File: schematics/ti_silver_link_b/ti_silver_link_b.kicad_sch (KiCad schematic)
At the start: 42 parts, among them P1 Conn_1x5, U1 24LC64, U2 TPS71533__SC70, U3 TUSB3410, U4 IMH8A, Y1 12MHz

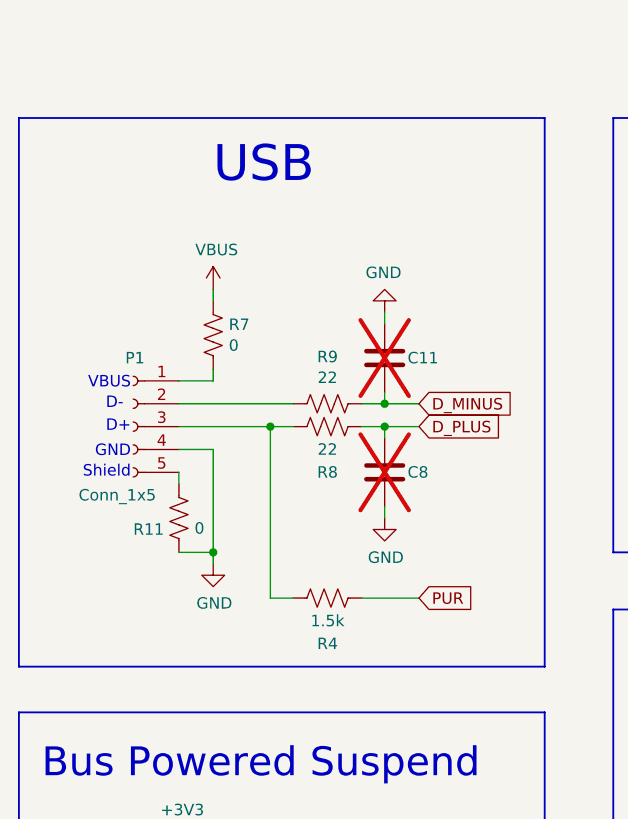
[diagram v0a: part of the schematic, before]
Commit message: Add footprints to "B" schematic's components and add initial pcb layout
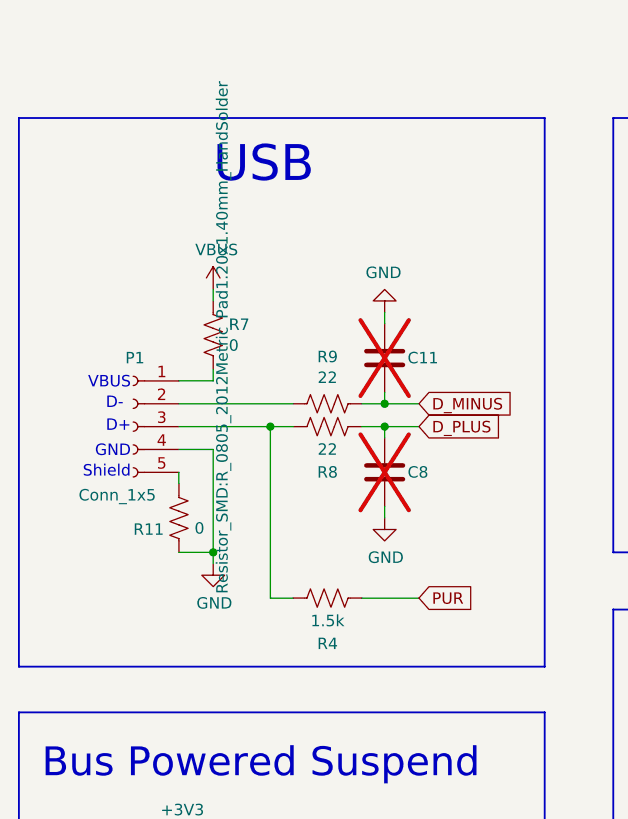
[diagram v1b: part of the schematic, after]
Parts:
- C1, C10, C11, C2, C3, C4, C5, C7, C8, C9: footprint (none) -> Capacitor_SMD:C_0805_2012Metric_Pad1.18x1.45mm_HandSolder
- D1: footprint (none) -> Package_TO_SOT_SMD:SOT-753
- L1, L2: footprint (none) -> Inductor_SMD:L_0805_2012Metric_Pad1.05x1.20mm_HandSolder
- P1: footprint (none) -> Connector_PinHeader_2.54mm:PinHeader_1x05_P2.54mm_Vertical
- R1, R10, R11, R2, R20, R21, R24, R25, R26, R27, R28, R29, R30, R4, R5, R6, R7, R8, R9: footprint (none) -> Resistor_SMD:R_0805_2012Metric_Pad1.20x1.40mm_HandSolder
- TI1: footprint (none) -> Connector_PinHeader_2.54mm:PinHeader_1x03_P2.54mm_Vertical
- TP1, TP2: footprint (none) -> TestPoint:TestPoint_Pad_D1.0mm
- U3: footprint Package_DFN_QFN:VQFN-32-1EP_5x5mm_P0.5mm_EP3.5x3.5mm_ThermalVias -> Package_QFP:LQFP-32_7x7mm_P0.8mm
- U4: footprint (none) -> Package_TO_SOT_SMD:SOT-457
- Y1: footprint (none) -> Crystal:Crystal_SMD_HC49-SD

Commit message: Update and fix "B" schematic's footprints and layout
Wrong pinout was used in U4 and D1
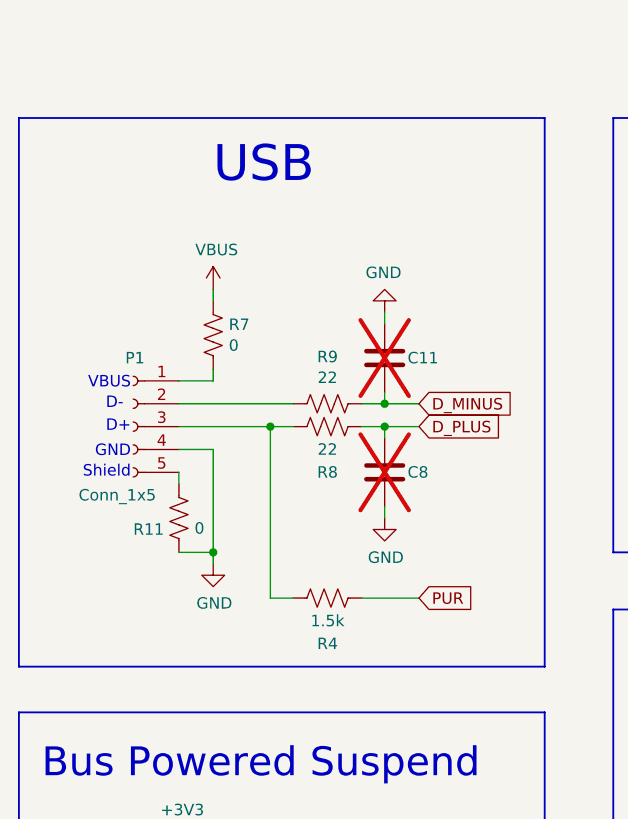
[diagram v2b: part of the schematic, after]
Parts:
- D1: footprint Package_TO_SOT_SMD:SOT-753 -> ti_graph_link_library:SOT-25_HandSoldering_clockwise_pin_numbering
- U4: footprint Package_TO_SOT_SMD:SOT-457 -> Package_TO_SOT_SMD:ROHM_SOT-457_ClockwisePinNumbering

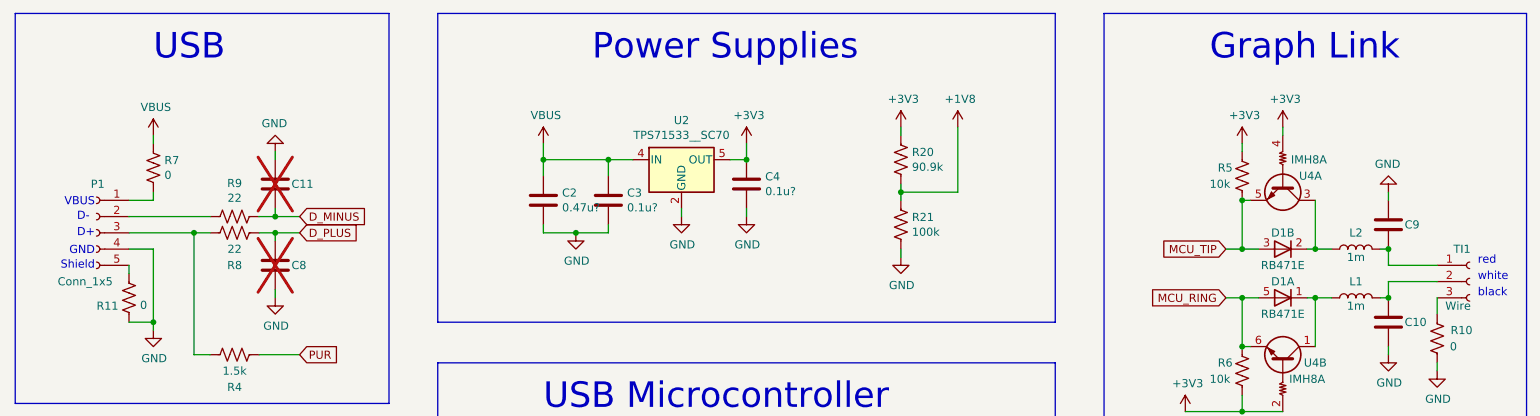
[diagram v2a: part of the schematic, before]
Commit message: Add USB and audio jack connectors to "B" schematic and pcb layout
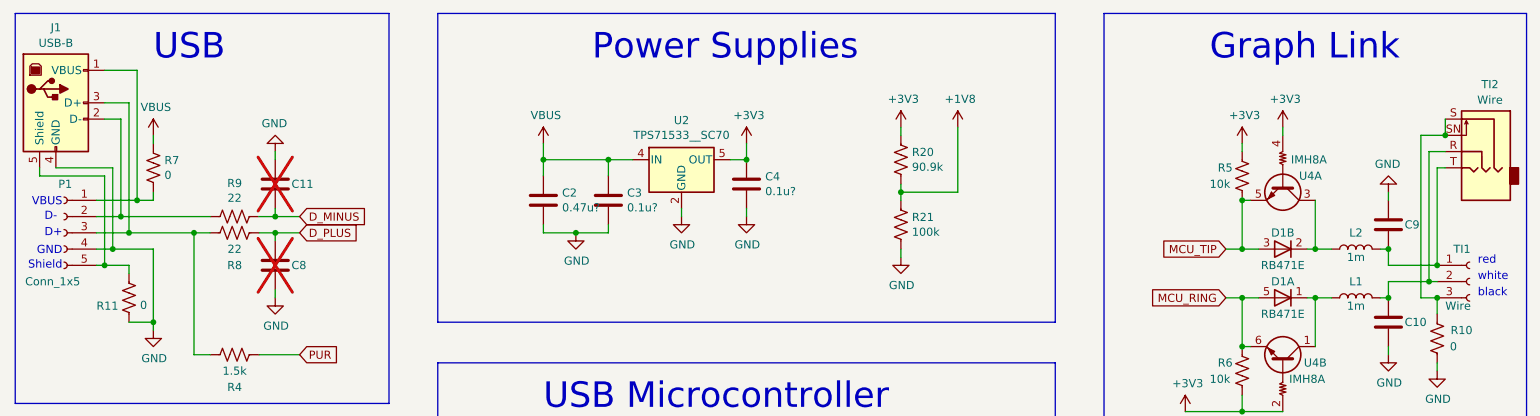
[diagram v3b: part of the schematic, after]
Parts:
- added J1: USB-B, ti_graph_link_library:USB_B_Logitech_C270_cable_connector, symbol ti_graph_link:USB-B
- added TI2: Wire, ti_graph_link_library:Jack_2.5mm_with_switch-SMT_Horizontal, symbol ti_graph_link:AudioJack3_SwitchS
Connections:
- net GND: now also J1.4 (GND)
- net at P1.1 (Pin_1), R7.2: now also J1.1 (VBUS)
- net at P1.2 (Pin_2), R9.2: now also J1.2 (D-)
- net at P1.3 (Pin_3), R4.2, R8.2: now also J1.3 (D+)
- net at P1.5 (Pin_5), R11.1: now also J1.5 (Shield)
- net at C9.2, L2.2, TI1.1 (Pin_1): now also TI2.T
- net at C10.1, L1.2, TI1.2 (Pin_2): now also TI2.R
- net at R10.1, TI1.3 (Pin_3): now also TI2.S, TI2.SN
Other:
- moved on the sheet: P1
